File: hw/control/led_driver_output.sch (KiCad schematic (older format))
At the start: 8 parts

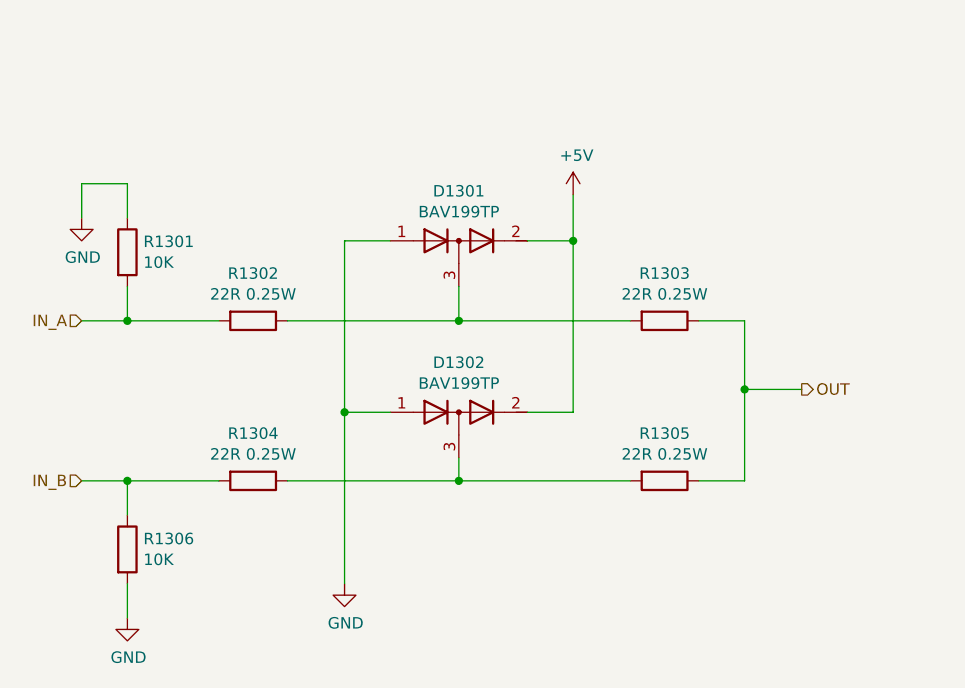
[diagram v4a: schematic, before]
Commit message: [hw] Add control board net classes
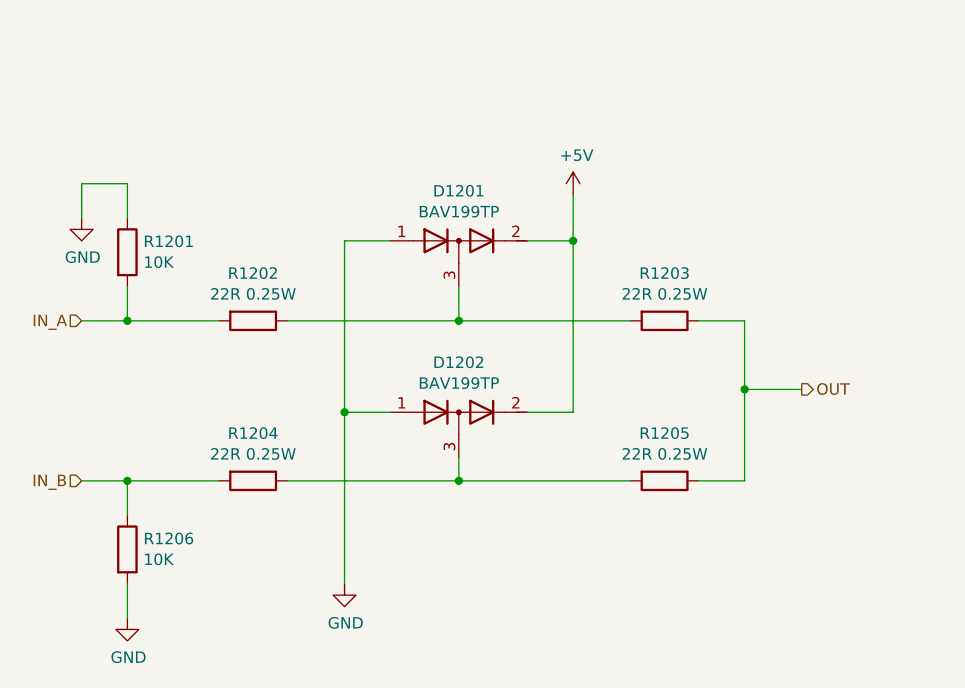
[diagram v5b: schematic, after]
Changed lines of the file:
@@
 $Descr A4 11693 8268
 encoding utf-8
-Sheet 13 13
+Sheet 12 13
 Title "WS2812 Controller"
 Date "2021-10-10"
@@
 AR Path="/614B1933/614A1815/614A3B39" Ref="R1202"  Part="1"
 AR Path="/614B1933/614AD8B5/614A3B39" Ref="R1302"  Part="1"
-F 0 "R1302" V 4743 3750 50  0000 C CNN
+F 0 "R1202" V 4743 3750 50  0000 C CNN
 F 1 "22R 0.25W" V 4834 3750 50  0000 C CNN
 F 2 "Resistor_SMD:R_1206_3216Metric_Pad1.30x1.75mm_HandSolder" V 4880 3750 50  0001 C CNN
@@
 AR Path="/614B1933/614A1815/614A3B3F" Ref="R1203"  Part="1"
 AR Path="/614B1933/614AD8B5/614A3B3F" Ref="R1303"  Part="1"
-F 0 "R1303" V 6543 3750 50  0000 C CNN
+F 0 "R1203" V 6543 3750 50  0000 C CNN
 F 1 "22R 0.25W" V 6634 3750 50  0000 C CNN
 F 2 "Resistor_SMD:R_1206_3216Metric_Pad1.30x1.75mm_HandSolder" V 6680 3750 50  0001 C CNN
@@
 AR Path="/614B1933/614A1815/614A3B45" Ref="R1204"  Part="1"
 AR Path="/614B1933/614AD8B5/614A3B45" Ref="R1304"  Part="1"
-F 0 "R1304" V 4743 4450 50  0000 C CNN
+F 0 "R1204" V 4743 4450 50  0000 C CNN
 F 1 "22R 0.25W" V 4834 4450 50  0000 C CNN
 F 2 "Resistor_SMD:R_1206_3216Metric_Pad1.30x1.75mm_HandSolder" V 4880 4450 50  0001 C CNN
@@
 AR Path="/614B1933/614A1815/614A3B4B" Ref="R1205"  Part="1"
 AR Path="/614B1933/614AD8B5/614A3B4B" Ref="R1305"  Part="1"
-F 0 "R1305" V 6543 4450 50  0000 C CNN
+F 0 "R1205" V 6543 4450 50  0000 C CNN
 F 1 "22R 0.25W" V 6634 4450 50  0000 C CNN
 F 2 "Resistor_SMD:R_1206_3216Metric_Pad1.30x1.75mm_HandSolder" V 6680 4450 50  0001 C CNN
@@
 AR Path="/614B1933/614A1815/614A3B51" Ref="D1201"  Part="1"
 AR Path="/614B1933/614AD8B5/614A3B51" Ref="D1301"  Part="1"
-F 0 "D1301" H 5850 3617 50  0000 C CNN
+F 0 "D1201" H 5850 3617 50  0000 C CNN
 F 1 "BAV199TP" H 5850 3526 50  0000 C CNN
 F 2 "Package_TO_SOT_SMD:SOT-23" H 5850 2900 50  0001 C CNN
@@
 AR Path="/614B1933/614A1815/614A3B57" Ref="D1202"  Part="1"
 AR Path="/614B1933/614AD8B5/614A3B57" Ref="D1302"  Part="1"
-F 0 "D1302" H 5850 4367 50  0000 C CNN
+F 0 "D1202" H 5850 4367 50  0000 C CNN
 F 1 "BAV199TP" H 5850 4276 50  0000 C CNN
 F 2 "Package_TO_SOT_SMD:SOT-23" H 5850 3650 50  0001 C CNN
@@
 AR Path="/614B1933/614A1815/616363D2" Ref="R1201"  Part="1"
 AR Path="/614B1933/614AD8B5/616363D2" Ref="R1301"  Part="1"
-F 0 "R1301" H 4470 3496 50  0000 L CNN
+F 0 "R1201" H 4470 3496 50  0000 L CNN
 F 1 "10K" H 4470 3405 50  0000 L CNN
 F 2 "Resistor_SMD:R_0805_2012Metric_Pad1.20x1.40mm_HandSolder" V 4330 3450 50  0001 C CNN
@@
 AR Path="/614B1933/614A1815/61637113" Ref="R1206"  Part="1"
 AR Path="/614B1933/614AD8B5/61637113" Ref="R1306"  Part="1"
-F 0 "R1306" H 4470 4796 50  0000 L CNN
+F 0 "R1206" H 4470 4796 50  0000 L CNN
 F 1 "10K" H 4470 4705 50  0000 L CNN
 F 2 "Resistor_SMD:R_0805_2012Metric_Pad1.20x1.40mm_HandSolder" V 4330 4750 50  0001 C CNN

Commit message: [hw] Incorporate suggestions
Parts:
- added C?: 100n, symbol Device:C
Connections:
- net +5V: now also C?.1
- net GND: now also C?.2
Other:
- note added: "Schotkyho diody, 5ns"
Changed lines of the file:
@@
 AR Path="/614B1933/614A1815/614A3B70" Ref="#PWR01201"  Part="1"
 AR Path="/614B1933/614AD8B5/614A3B70" Ref="#PWR01301"  Part="1"
-F 0 "#PWR01301" H 6350 3050 50  0001 C CNN
+F 0 "#PWR01201" H 6350 3050 50  0001 C CNN
 F 1 "+5V" H 6365 3373 50  0000 C CNN
 F 2 "" H 6350 3200 50  0001 C CNN
@@
 AR Path="/614B1933/614A1815/614A4F14" Ref="#PWR01203"  Part="1"
 AR Path="/614B1933/614AD8B5/614A4F14" Ref="#PWR01303"  Part="1"
-F 0 "#PWR01303" H 5350 4650 50  0001 C CNN
+F 0 "#PWR01203" H 5350 4650 50  0001 C CNN
 F 1 "GND" H 5355 4727 50  0000 C CNN
 F 2 "" H 5350 4900 50  0001 C CNN
@@
 AR Path="/614B1933/614A1815/61637D81" Ref="#PWR01202"  Part="1"
 AR Path="/614B1933/614AD8B5/61637D81" Ref="#PWR01302"  Part="1"
-F 0 "#PWR01302" H 4200 3050 50  0001 C CNN
+F 0 "#PWR01202" H 4200 3050 50  0001 C CNN
 F 1 "GND" H 4205 3127 50  0000 C CNN
 F 2 "" H 4200 3300 50  0001 C CNN
@@
 AR Path="/614B1933/614A1815/6163895E" Ref="#PWR01204"  Part="1"
 AR Path="/614B1933/614AD8B5/6163895E" Ref="#PWR01304"  Part="1"
-F 0 "#PWR01304" H 4400 4800 50  0001 C CNN
+F 0 "#PWR01204" H 4400 4800 50  0001 C CNN
 F 1 "GND" H 4405 4877 50  0000 C CNN
 F 2 "" H 4400 5050 50  0001 C CNN
@@
 Wire Wire Line
 	4200 3150 4200 3300
+$Comp
+L Device:C C?
+U 1 1 616BDFA1
+P 7650 3300
+F 0 "C?" H 7765 3346 50  0000 L CNN
+F 1 "100n" H 7765 3255 50  0000 L CNN
+F 2 "" H 7688 3150 50  0001 C CNN
+F 3 "~" H 7650 3300 50  0001 C CNN
+	1    7650 3300
+	1    0    0    -1
+$EndComp
+$Comp
+L power:GND #PWR?
+U 1 1 616BEE8A
+P 7650 3450
+F 0 "#PWR?" H 7650 3200 50  0001 C CNN
+F 1 "GND" H 7655 3277 50  0000 C CNN
+F 2 "" H 7650 3450 50  0001 C CNN
+F 3 "" H 7650 3450 50  0001 C CNN
+	1    7650 3450
+	1    0    0    -1
+$EndComp
+Wire Wire Line
+	7650 3150 6650 3150
+Wire Wire Line
+	6650 3150 6650 3400
+Wire Wire Line
+	6650 3400 6350 3400
+Text Notes 5650 4600 0    50   ~ 0
+Schotkyho diody, 5ns
 $EndSCHEMATC

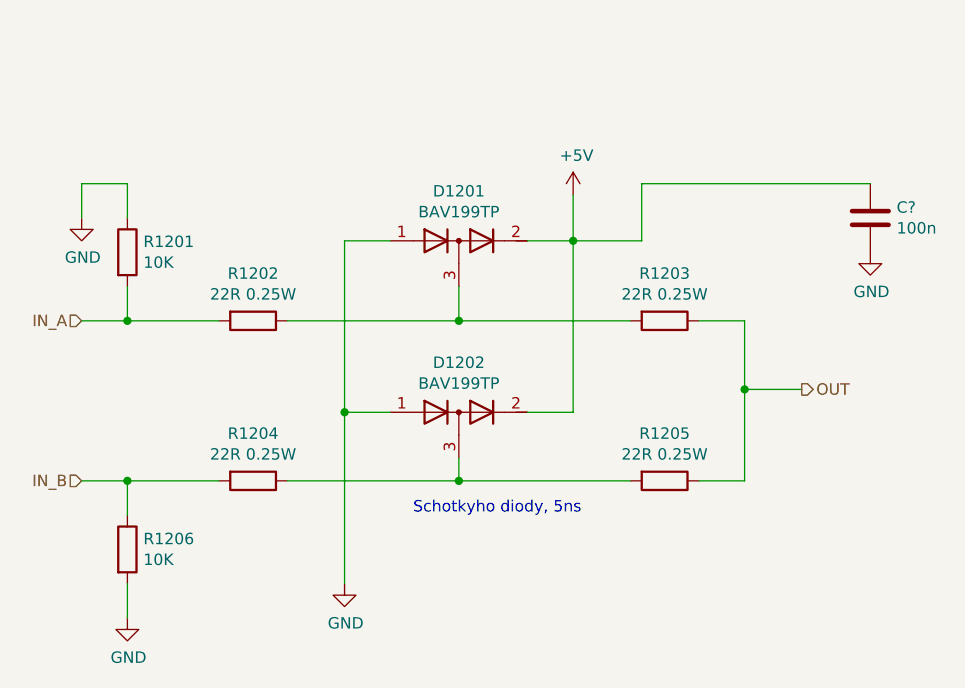
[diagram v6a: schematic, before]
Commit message: [hw] Assign control board footprints
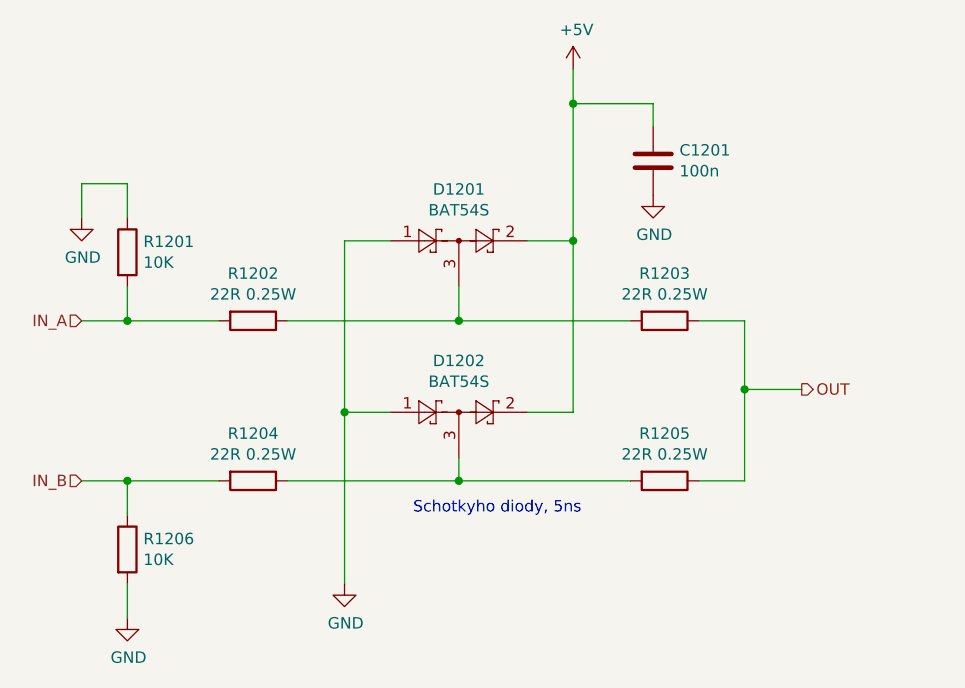
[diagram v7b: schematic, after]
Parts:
- removed D1201, D1202: BAV199TP, Package_TO_SOT_SMD:SOT-23, symbol my:BAV199TP
- added D1201, D1202: BAT54S, Package_TO_SOT_SMD:SOT-23, symbol Diode:BAT54S
- C1201: renamed from C?; footprint (none) -> Capacitor_SMD:C_0805_2012Metric_Pad1.18x1.45mm_HandSolder
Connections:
- net +5V: now also D1201.2, D1202.2
- net GND: now also D1201.1, D1202.1
- net at R1202.1, R1203.2: now also D1201.3
- net at R1204.1, R1205.2: now also D1202.3
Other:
- moved on the sheet: C1201
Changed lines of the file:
@@
 	0    1    1    0
-$EndComp
-$Comp
-L my:BAV199TP D?
-U 1 1 614A3B51
-P 5850 3400
-AR Path="/614B1933/614A3B51" Ref="D?"  Part="1"
-AR Path="/614B1933/614A1815/614A3B51" Ref="D1201"  Part="1"
-AR Path="/614B1933/614AD8B5/614A3B51" Ref="D1301"  Part="1"
-F 0 "D1201" H 5850 3617 50  0000 C CNN
-F 1 "BAV199TP" H 5850 3526 50  0000 C CNN
-F 2 "Package_TO_SOT_SMD:SOT-23" H 5850 2900 50  0001 C CNN
-F 3 "https://www.diodes.com/assets/Datasheets/ds30232.pdf" H 5850 3400 50  0001 C CNN
-	1    5850 3400
-	1    0    0    -1
-$EndComp
-$Comp
-L my:BAV199TP D?
-U 1 1 614A3B57
-P 5850 4150
-AR Path="/614B1933/614A3B57" Ref="D?"  Part="1"
-AR Path="/614B1933/614A1815/614A3B57" Ref="D1202"  Part="1"
-AR Path="/614B1933/614AD8B5/614A3B57" Ref="D1302"  Part="1"
-F 0 "D1202" H 5850 4367 50  0000 C CNN
-F 1 "BAV199TP" H 5850 4276 50  0000 C CNN
-F 2 "Package_TO_SOT_SMD:SOT-23" H 5850 3650 50  0001 C CNN
-F 3 "https://www.diodes.com/assets/Datasheets/ds30232.pdf" H 5850 4150 50  0001 C CNN
-	1    5850 4150
-	1    0    0    -1
 $EndComp
 Wire Wire Line
@@
 L power:+5V #PWR?
 U 1 1 614A3B70
-P 6350 3200
+P 6350 2650
 AR Path="/614B1933/614A3B70" Ref="#PWR?"  Part="1"
 AR Path="/614B1933/614A1815/614A3B70" Ref="#PWR01201"  Part="1"
 AR Path="/614B1933/614AD8B5/614A3B70" Ref="#PWR01301"  Part="1"
-F 0 "#PWR01201" H 6350 3050 50  0001 C CNN
-F 1 "+5V" H 6365 3373 50  0000 C CNN
-F 2 "" H 6350 3200 50  0001 C CNN
-F 3 "" H 6350 3200 50  0001 C CNN
-	1    6350 3200
-	1    0    0    -1
-$EndComp
-Wire Wire Line
-	6350 3200 6350 3400
+F 0 "#PWR01301" H 6350 2500 50  0001 C CNN
+F 1 "+5V" H 6365 2823 50  0000 C CNN
+F 2 "" H 6350 2650 50  0001 C CNN
+F 3 "" H 6350 2650 50  0001 C CNN
+	1    6350 2650
+	1    0    0    -1
+$EndComp
+Wire Wire Line
+	6350 2650 6350 2800
 Wire Wire Line
 	6350 3400 6150 3400
@@
 AR Path="/614B1933/614A1815/614A4F14" Ref="#PWR01203"  Part="1"
 AR Path="/614B1933/614AD8B5/614A4F14" Ref="#PWR01303"  Part="1"
-F 0 "#PWR01203" H 5350 4650 50  0001 C CNN
+F 0 "#PWR01303" H 5350 4650 50  0001 C CNN
 F 1 "GND" H 5355 4727 50  0000 C CNN
 F 2 "" H 5350 4900 50  0001 C CNN
@@
 AR Path="/614B1933/614A1815/61637D81" Ref="#PWR01202"  Part="1"
 AR Path="/614B1933/614AD8B5/61637D81" Ref="#PWR01302"  Part="1"
-F 0 "#PWR01202" H 4200 3050 50  0001 C CNN
+F 0 "#PWR01302" H 4200 3050 50  0001 C CNN
 F 1 "GND" H 4205 3127 50  0000 C CNN
 F 2 "" H 4200 3300 50  0001 C CNN
@@
 AR Path="/614B1933/614A1815/6163895E" Ref="#PWR01204"  Part="1"
 AR Path="/614B1933/614AD8B5/6163895E" Ref="#PWR01304"  Part="1"
-F 0 "#PWR01204" H 4400 4800 50  0001 C CNN
+F 0 "#PWR01304" H 4400 4800 50  0001 C CNN
 F 1 "GND" H 4405 4877 50  0000 C CNN
 F 2 "" H 4400 5050 50  0001 C CNN
@@
 	4200 3150 4200 3300
 $Comp
-L Device:C C?
+L Device:C C1201
 U 1 1 616BDFA1
-P 7650 3300
-F 0 "C?" H 7765 3346 50  0000 L CNN
-F 1 "100n" H 7765 3255 50  0000 L CNN
-F 2 "" H 7688 3150 50  0001 C CNN
-F 3 "~" H 7650 3300 50  0001 C CNN
-	1    7650 3300
-	1    0    0    -1
-$EndComp
-$Comp
-L power:GND #PWR?
+P 6700 3050
+AR Path="/614B1933/614A1815/616BDFA1" Ref="C1201"  Part="1"
+AR Path="/614B1933/614AD8B5/616BDFA1" Ref="C1301"  Part="1"
+F 0 "C1201" H 6815 3096 50  0000 L CNN
+F 1 "100n" H 6815 3005 50  0000 L CNN
+F 2 "Capacitor_SMD:C_0805_2012Metric_Pad1.18x1.45mm_HandSolder" H 6738 2900 50  0001 C CNN
+F 3 "~" H 6700 3050 50  0001 C CNN
+	1    6700 3050
+	1    0    0    -1
+$EndComp
+$Comp
+L power:GND #PWR01205
 U 1 1 616BEE8A
-P 7650 3450
-F 0 "#PWR?" H 7650 3200 50  0001 C CNN
-F 1 "GND" H 7655 3277 50  0000 C CNN
-F 2 "" H 7650 3450 50  0001 C CNN
-F 3 "" H 7650 3450 50  0001 C CNN
-	1    7650 3450
-	1    0    0    -1
-$EndComp
-Wire Wire Line
-	7650 3150 6650 3150
-Wire Wire Line
-	6650 3150 6650 3400
-Wire Wire Line
-	6650 3400 6350 3400
+P 6700 3200
+AR Path="/614B1933/614A1815/616BEE8A" Ref="#PWR01205"  Part="1"
+AR Path="/614B1933/614AD8B5/616BEE8A" Ref="#PWR01305"  Part="1"
+F 0 "#PWR01305" H 6700 2950 50  0001 C CNN
+F 1 "GND" H 6705 3027 50  0000 C CNN
+F 2 "" H 6700 3200 50  0001 C CNN
+F 3 "" H 6700 3200 50  0001 C CNN
+	1    6700 3200
+	1    0    0    -1
+$EndComp
 Text Notes 5650 4600 0    50   ~ 0
 Schotkyho diody, 5ns
+$Comp
+L Diode:BAT54S D1201
+U 1 1 616B883B
+P 5850 3400
+AR Path="/614B1933/614A1815/616B883B" Ref="D1201"  Part="1"
+AR Path="/614B1933/614AD8B5/616B883B" Ref="D1301"  Part="1"
+F 0 "D1201" H 5850 3625 50  0000 C CNN
+F 1 "BAT54S" H 5850 3534 50  0000 C CNN
+F 2 "Package_TO_SOT_SMD:SOT-23" H 5925 3525 50  0001 L CNN
+F 3 "https://www.diodes.com/assets/Datasheets/ds11005.pdf" H 5730 3400 50  0001 C CNN
+	1    5850 3400
+	1    0    0    -1
+$EndComp
+$Comp
+L Diode:BAT54S D1202
+U 1 1 616B92EE
+P 5850 4150
+AR Path="/614B1933/614A1815/616B92EE" Ref="D1202"  Part="1"
+AR Path="/614B1933/614AD8B5/616B92EE" Ref="D1302"  Part="1"
+F 0 "D1202" H 5850 4375 50  0000 C CNN
+F 1 "BAT54S" H 5850 4284 50  0000 C CNN
+F 2 "Package_TO_SOT_SMD:SOT-23" H 5925 4275 50  0001 L CNN
+F 3 "https://www.diodes.com/assets/Datasheets/ds11005.pdf" H 5730 4150 50  0001 C CNN
+	1    5850 4150
+	1    0    0    -1
+$EndComp
+Wire Wire Line
+	6700 2900 6700 2800
+Wire Wire Line
+	6700 2800 6350 2800
+Connection ~ 6350 2800
+Wire Wire Line
+	6350 2800 6350 3400
 $EndSCHEMATC

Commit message: [hw] Calculate some values in control board
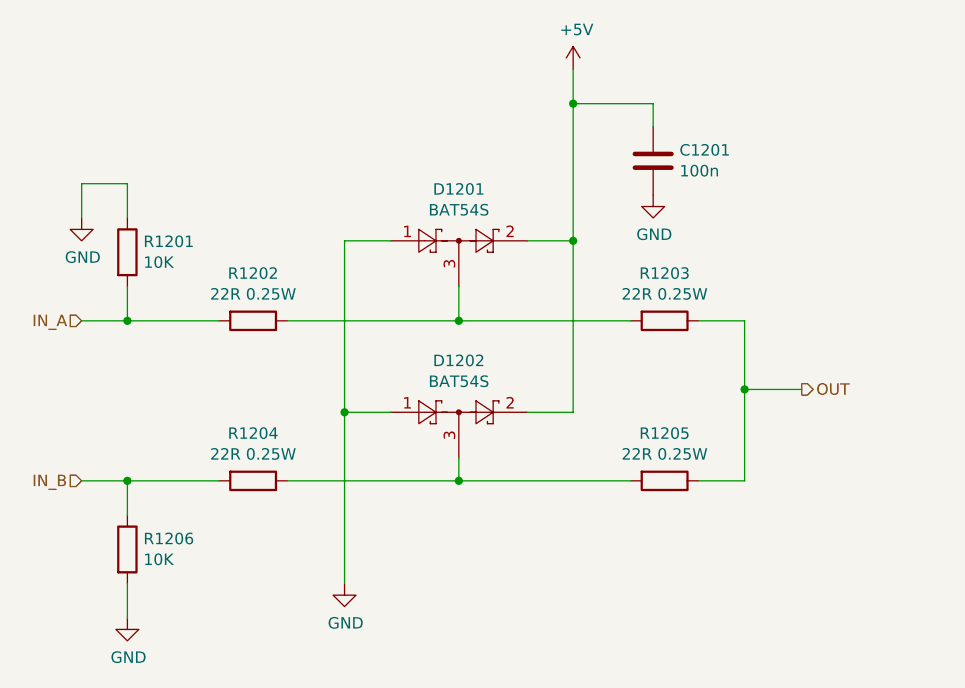
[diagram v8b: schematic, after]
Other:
- note removed: "Schotkyho diody, 5ns"
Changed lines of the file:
@@
 AR Path="/614B1933/614A1815/614A3B70" Ref="#PWR01201"  Part="1"
 AR Path="/614B1933/614AD8B5/614A3B70" Ref="#PWR01301"  Part="1"
-F 0 "#PWR01301" H 6350 2500 50  0001 C CNN
+F 0 "#PWR01201" H 6350 2500 50  0001 C CNN
 F 1 "+5V" H 6365 2823 50  0000 C CNN
 F 2 "" H 6350 2650 50  0001 C CNN
@@
 AR Path="/614B1933/614A1815/614A4F14" Ref="#PWR01203"  Part="1"
 AR Path="/614B1933/614AD8B5/614A4F14" Ref="#PWR01303"  Part="1"
-F 0 "#PWR01303" H 5350 4650 50  0001 C CNN
+F 0 "#PWR01203" H 5350 4650 50  0001 C CNN
 F 1 "GND" H 5355 4727 50  0000 C CNN
 F 2 "" H 5350 4900 50  0001 C CNN
@@
 AR Path="/614B1933/614A1815/61637D81" Ref="#PWR01202"  Part="1"
 AR Path="/614B1933/614AD8B5/61637D81" Ref="#PWR01302"  Part="1"
-F 0 "#PWR01302" H 4200 3050 50  0001 C CNN
+F 0 "#PWR01202" H 4200 3050 50  0001 C CNN
 F 1 "GND" H 4205 3127 50  0000 C CNN
 F 2 "" H 4200 3300 50  0001 C CNN
@@
 AR Path="/614B1933/614A1815/6163895E" Ref="#PWR01204"  Part="1"
 AR Path="/614B1933/614AD8B5/6163895E" Ref="#PWR01304"  Part="1"
-F 0 "#PWR01304" H 4400 4800 50  0001 C CNN
+F 0 "#PWR01204" H 4400 4800 50  0001 C CNN
 F 1 "GND" H 4405 4877 50  0000 C CNN
 F 2 "" H 4400 5050 50  0001 C CNN
@@
 AR Path="/614B1933/614A1815/616BEE8A" Ref="#PWR01205"  Part="1"
 AR Path="/614B1933/614AD8B5/616BEE8A" Ref="#PWR01305"  Part="1"
-F 0 "#PWR01305" H 6700 2950 50  0001 C CNN
+F 0 "#PWR01205" H 6700 2950 50  0001 C CNN
 F 1 "GND" H 6705 3027 50  0000 C CNN
 F 2 "" H 6700 3200 50  0001 C CNN
@@
 	1    0    0    -1
 $EndComp
-Text Notes 5650 4600 0    50   ~ 0
-Schotkyho diody, 5ns
 $Comp
 L Diode:BAT54S D1201
